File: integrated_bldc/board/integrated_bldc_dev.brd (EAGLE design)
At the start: 81.9 x 49.4 mm, 107 parts, among them J2 PRG

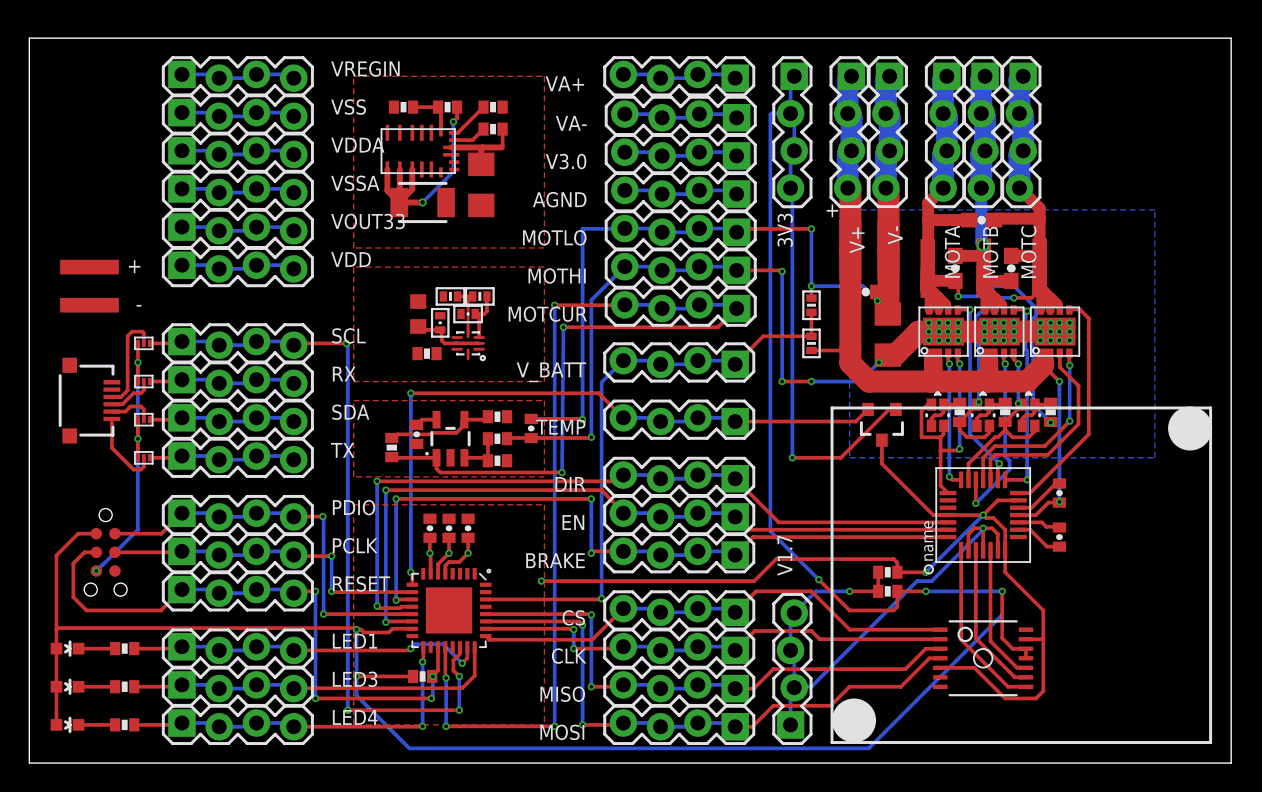
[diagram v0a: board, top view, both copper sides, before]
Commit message: Finished Dev board layout. Added stop mask to vias. Corrected some component values based on part order.
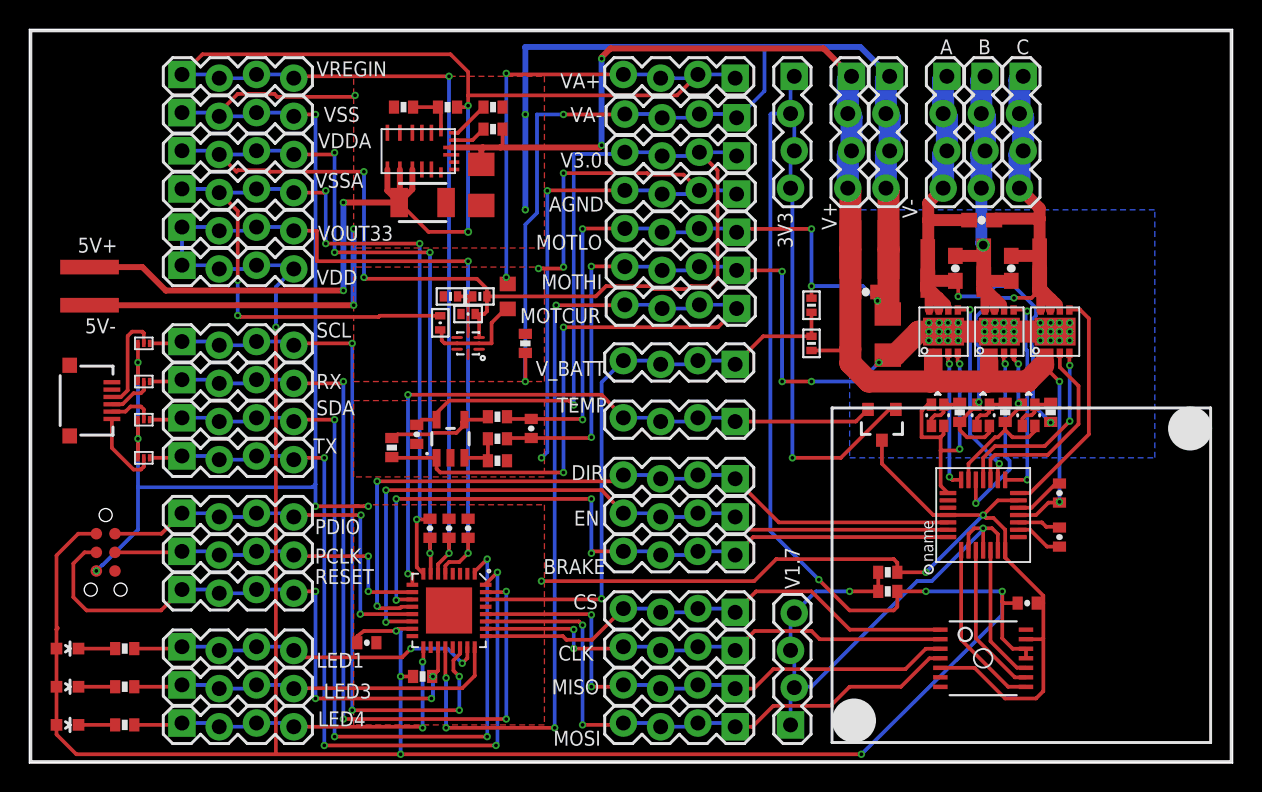
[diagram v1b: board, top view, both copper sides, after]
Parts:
- added C14, C6: 0.1uF, SparkFun-Passives:0402-CAP
- added U$16: (no value), modular_robotics:INFO
- D12: value GREEN -> WHITE
- R26: value 40k -> 39k
- moved R24 6.74 mm to (33.8, 28.6), turned to 270 degrees
- moved R17 6.22 mm to (32.6, 31.8)
- renumbered MOTA to A, MOTB to B, MOTC to C
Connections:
- net +3V3: now also C14.1, C6.1
- net GND: now also C14.2, C6.2
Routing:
- net GND: track 166.4 -> 314.6 mm, vias 10 -> 21
- net +5V: track 35.2 -> 173.4 mm, vias 3 -> 8
- net V_3.0: track 23.5 -> 143.4 mm, vias 1 -> 7
- net AGND: track 15.9 -> 116.1 mm, vias 0 -> 11
- net +3V3: track 207.5 -> 280.5 mm, vias 7 -> 11
- net I2C_SDA: track 10.2 -> 58.5 mm, vias 0 -> 4
- net UART_RX: track 10.2 -> 57.8 mm, vias 0 -> 4
- net UART_TX: track 10.2 -> 56.6 mm, vias 0 -> 4
- net V+: track 63.5 -> 94.4 mm, vias 2 -> 4
- net N$15: track 4.99 -> 7.14 mm
- net MOTGND: track 55.5 -> 56.8 mm, vias 41 -> 42
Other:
- board size 81.9 x 49.4 mm -> 82 x 50 mm
- board text added: "5V+"
- board text added: "5V-"
- board text removed: "+"
- board text removed: "-"

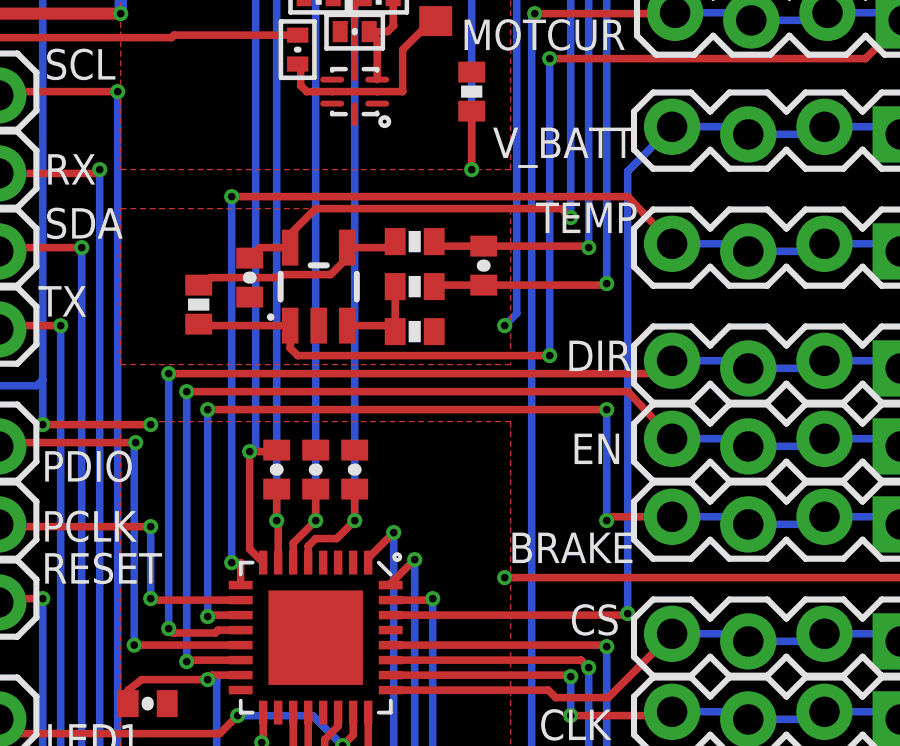
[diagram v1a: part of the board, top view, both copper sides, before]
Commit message: Fixed spacing on DC-DC converter, updated all polygons to 0.15mm isolate for good measure.
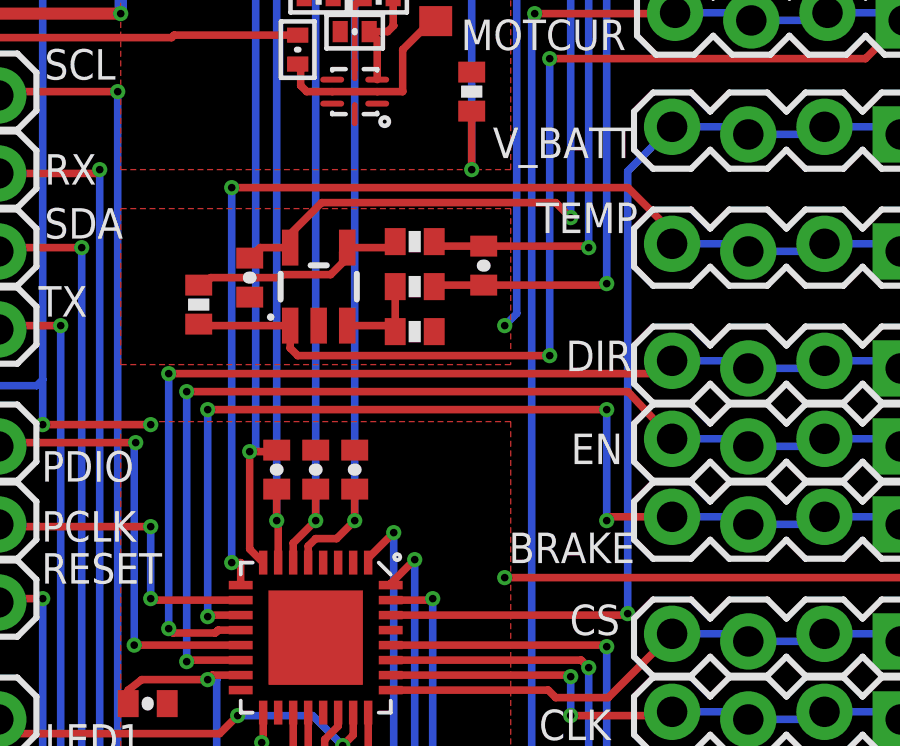
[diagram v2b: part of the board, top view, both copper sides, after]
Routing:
- net TEMP: track 45.9 -> 46.6 mm
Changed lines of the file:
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@@
 <?xml version="1.0" encoding="utf-8"?>
 <!DOCTYPE eagle SYSTEM "eagle.dtd">
-<eagle version="6.6.0">
+<eagle version="6.5.0">
 <drawing>
 <settings>
@@
 <layer number="14" name="Route14" color="1" fill="6" visible="no" active="no"/>
 <layer number="15" name="Route15" color="4" fill="6" visible="no" active="no"/>
-<layer number="16" name="Bottom" color="1" fill="1" visible="no" active="yes"/>
+<layer number="16" name="Bottom" color="1" fill="1" visible="yes" active="yes"/>
 <layer number="17" name="Pads" color="2" fill="1" visible="yes" active="yes"/>
 <layer number="18" name="Vias" color="2" fill="1" visible="yes" active="yes"/>
 <layer number="19" name="Unrouted" color="6" fill="1" visible="yes" active="yes"/>
 <layer number="20" name="Dimension" color="15" fill="1" visible="yes" active="yes"/>
-<layer number="21" name="tPlace" color="7" fill="1" visible="yes" active="yes"/>
+<layer number="21" name="tPlace" color="7" fill="1" visible="no" active="yes"/>
 <layer number="22" name="bPlace" color="7" fill="1" visible="no" active="yes"/>
-<layer number="23" name="tOrigins" color="15" fill="1" visible="yes" active="yes"/>
+<layer number="23" name="tOrigins" color="15" fill="1" visible="no" active="yes"/>
 <layer number="24" name="bOrigins" color="15" fill="1" visible="no" active="yes"/>
 <layer number="25" name="tNames" color="7" fill="1" visible="no" active="yes"/>
@@
 <layer number="27" name="tValues" color="7" fill="1" visible="no" active="yes"/>
 <layer number="28" name="bValues" color="7" fill="1" visible="no" active="yes"/>
-<layer number="29" name="tStop" color="7" fill="3" visible="yes" active="yes"/>
+<layer number="29" name="tStop" color="7" fill="3" visible="no" active="yes"/>
 <layer number="30" name="bStop" color="7" fill="6" visible="no" active="yes"/>
 <layer number="31" name="tCream" color="7" fill="4" visible="no" active="yes"/>
@@
 <layer number="37" name="tTest" color="7" fill="1" visible="no" active="yes"/>
 <layer number="38" name="bTest" color="7" fill="1" visible="no" active="yes"/>
-<layer number="39" name="tKeepout" color="4" fill="11" visible="yes" active="yes"/>
+<layer number="39" name="tKeepout" color="4" fill="11" visible="no" active="yes"/>
 <layer number="40" name="bKeepout" color="1" fill="11" visible="no" active="yes"/>
 <layer number="41" name="tRestrict" color="4" fill="10" visible="no" active="yes"/>
@@
 <layer number="46" name="Milling" color="3" fill="1" visible="no" active="yes"/>
 <layer number="47" name="Measures" color="7" fill="1" visible="no" active="yes"/>
-<layer number="48" name="Document" color="7" fill="1" visible="yes" active="yes"/>
+<layer number="48" name="Document" color="7" fill="1" visible="no" active="yes"/>
 <layer number="49" name="Reference" color="7" fill="1" visible="no" active="yes"/>
 <layer number="50" name="dxf" color="7" fill="1" visible="no" active="no"/>
-<layer number="51" name="tDocu" color="7" fill="1" visible="yes" active="yes"/>
+<layer number="51" name="tDocu" color="7" fill="1" visible="no" active="yes"/>
 <layer number="52" name="bDocu" color="7" fill="1" visible="no" active="yes"/>
 <layer number="53" name="tGND_GNDA" color="7" fill="9" visible="no" active="no"/>
@@
 <contactref element="C17" pad="1"/>
 <contactref element="R20" pad="2"/>
-<polygon width="0.254" layer="1">
+<polygon width="0.254" layer="1" isolate="0.15">
 <vertex x="22.1" y="46.8"/>
 <vertex x="35.1" y="46.8"/>
@@
 <wire x1="26.1" y1="12.9" x2="25.8" y2="12.9" width="0.254" layer="1"/>
 <via x="25.8" y="12.9" extent="1-16" drill="0.254"/>
-<wire x1="25.8" y1="12.9" x2="25.8" y2="25.1" width="0.254" layer="16"/>
-<via x="25.8" y="25.1" extent="1-16" drill="0.254"/>
-<wire x1="25.8" y1="25.1" x2="39.007" y2="25.1" width="0.254" layer="1"/>
-<wire x1="39.007" y1="25.1" x2="40.48" y2="23.527" width="0.254" layer="1"/>
+<wire x1="25.8" y1="12.9" x2="25.8" y2="25.4" width="0.254" layer="16"/>
+<via x="25.8" y="25.4" extent="1-16" drill="0.254"/>
+<wire x1="25.8" y1="25.4" x2="39.007" y2="25.4" width="0.254" layer="1"/>
 <wire x1="48.1" y1="23.273" x2="56.323" y2="23.273" width="0.254" layer="1"/>
 <wire x1="56.323" y1="23.273" x2="57.15" y2="24.1" width="0.254" layer="1"/>
+<wire x1="39.007" y1="25.4" x2="40.48" y2="23.927" width="0.254" layer="1"/>
+<wire x1="40.48" y1="23.927" x2="40.48" y2="23.527" width="0.254" layer="1"/>
 </signal>
 <signal name="N$4">
@@
 <contactref element="R16" pad="1"/>
 <contactref element="C13" pad="2"/>
-<polygon width="0.254" layer="1" rank="2">
+<polygon width="0.254" layer="1" isolate="0.15" rank="2">
 <vertex x="22.1" y="24.7"/>
 <vertex x="35.1" y="24.7"/>
@@
 <vertex x="22.1" y="19.5"/>
 </polygon>
-<polygon width="0.254" layer="1">
+<polygon width="0.254" layer="1" isolate="0.15">
 <vertex x="35.1" y="33.8"/>
 <vertex x="22.1" y="33.8"/>
@@
 <wire x1="46.9" y1="40.387" x2="45.66" y2="41.627" width="0.254" layer="1"/>
 <wire x1="27.75" y1="23.4001" x2="27.75" y2="23.85" width="0.254" layer="1"/>
-<wire x1="27.75" y1="23.85" x2="28.6" y2="24.7" width="0.254" layer="1"/>
-<wire x1="28.6" y1="24.7" x2="36.8" y2="24.7" width="0.254" layer="1"/>
-<wire x1="36.8" y1="24.7" x2="37.1" y2="24.4" width="0.254" layer="1"/>
+<wire x1="27.75" y1="23.85" x2="28.8" y2="24.9" width="0.254" layer="1"/>
+<wire x1="28.8" y1="24.9" x2="36.6" y2="24.9" width="0.254" layer="1"/>
+<wire x1="36.6" y1="24.9" x2="37.1" y2="24.4" width="0.254" layer="1"/>
 <via x="37.1" y="24.4" extent="1-16" drill="0.254"/>
 <wire x1="37.1" y1="24.4" x2="37.1" y2="41.5" width="0.254" layer="16"/>
@@
 <wire x1="38.3" y1="22.2" x2="38.3" y2="33.847" width="0.254" layer="16"/>
 <via x="57.9" y="27.3" extent="1-16" drill="0.254"/>
-<polygon width="0.254" layer="16">
+<polygon width="0.254" layer="16" isolate="0.15">
 <vertex x="55.9" y="20.8"/>
 <vertex x="76.7" y="20.8"/>
